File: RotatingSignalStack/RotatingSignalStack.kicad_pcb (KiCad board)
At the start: 2 copper layers, 64.1 x 54 mm, 96 parts, among them IC2 STM32H562RIT6, J1 Conn_01x06, J2 Conn_01x04, J3 RJ45_LED_Shielded, J4 Conn_01x09, SW1 SW_Push, SW5 SW_Push, SW6 SW_Push, SW7 SW_Push, T1 GMG116S1202R, U1 TMAG5273C1QDBVR, U2 AP63203WU-7, U3 SN65HVD232, U4 DP83825I, U5 SG-210STF 50.0000ML0, U6 USBLC6-2SC6, U7 USBLC6-4SC6, U8 OKI-78SR-3.3_1.5-W36-C

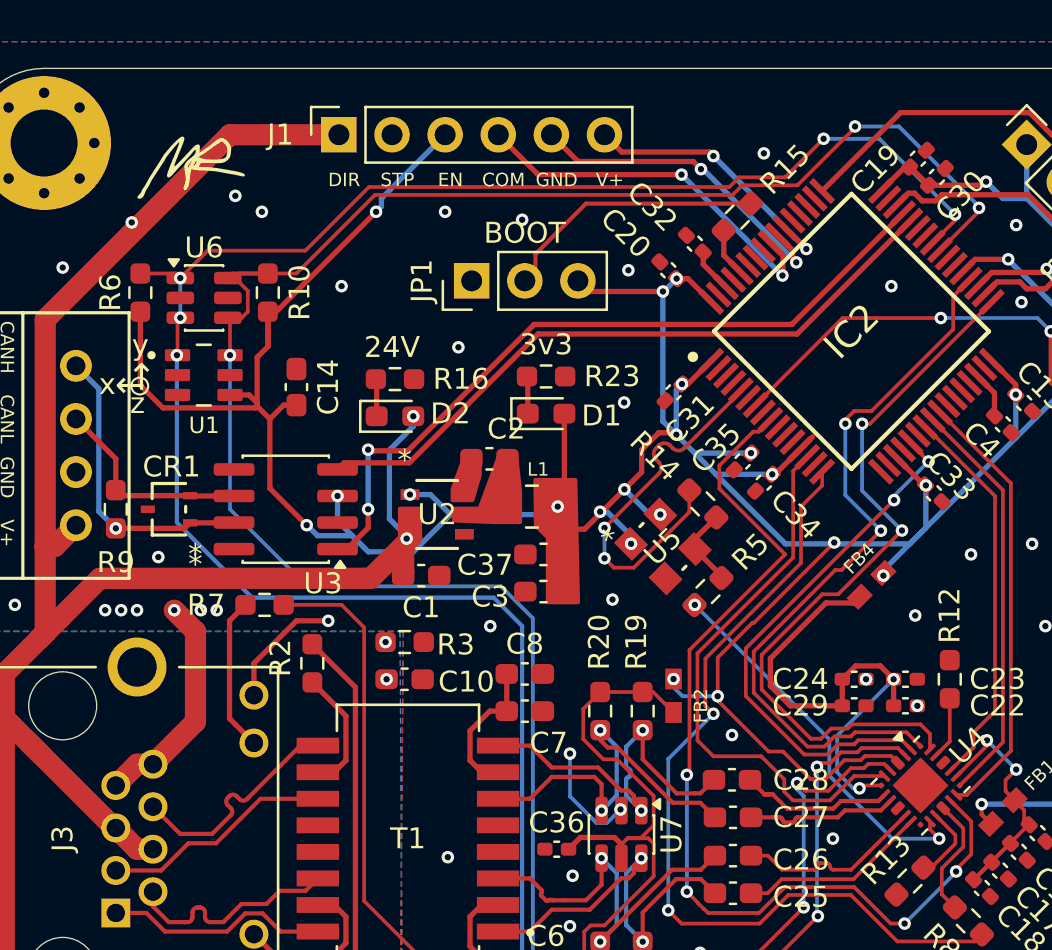
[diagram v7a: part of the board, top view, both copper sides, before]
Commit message: some more vias
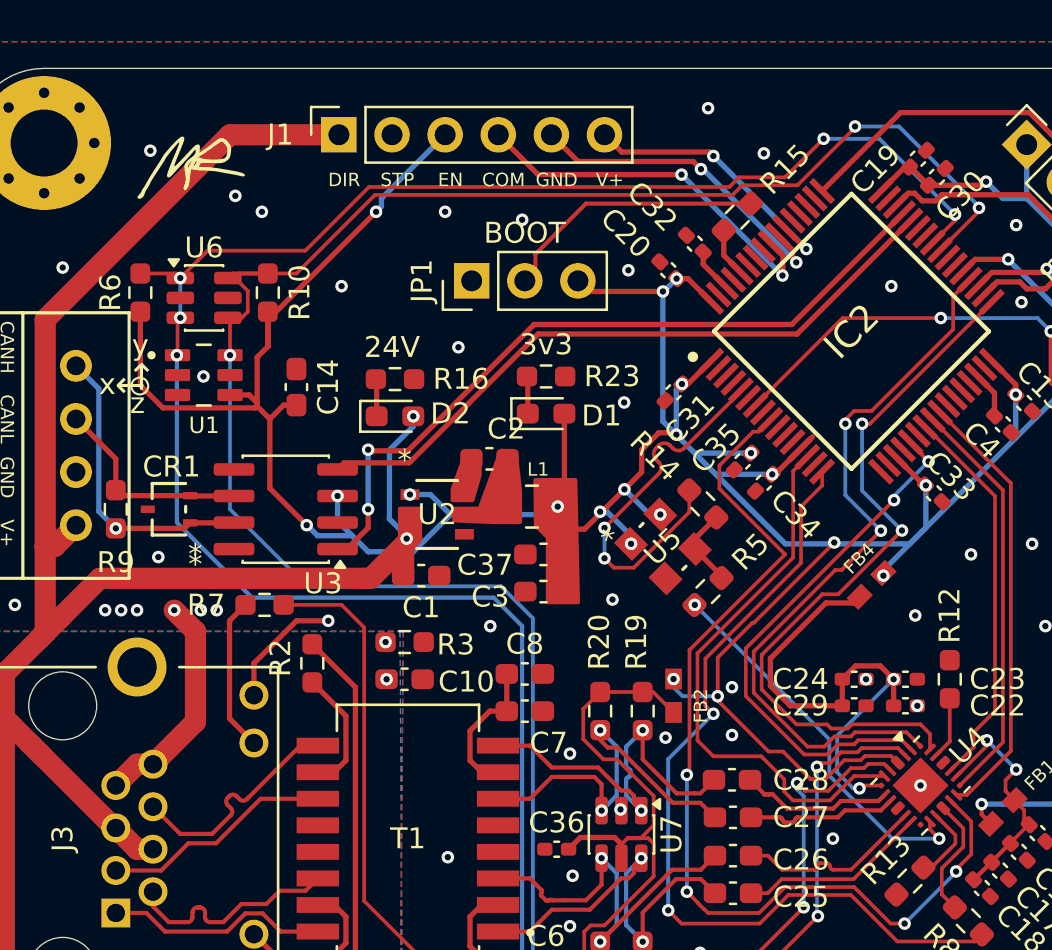
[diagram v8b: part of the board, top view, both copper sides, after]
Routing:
- net GND: track 28.8 -> 23.6 mm, vias 51 -> 56
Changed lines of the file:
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@@
 	)
 	(via
+		(at 161.798 84.709)
+		(size 0.6)
+		(drill 0.3)
+		(layers "F.Cu" "B.Cu")
+		(free yes)
+		(net 1)
+	)
+	(via
 		(at 156.083 80.518)
 		(size 0.6)
@@
 	)
 	(via
+		(at 170.815 89.408)
+		(size 0.6)
+		(drill 0.3)
+		(layers "F.Cu" "B.Cu")
+		(net 1)
+	)
+	(via
 		(at 169.418 65.532)
 		(size 0.6)
@@
 	)
 	(via
-		(at 133.096 62.484)
+		(at 133.985 59.055)
+		(size 0.6)
+		(drill 0.3)
+		(layers "F.Cu" "B.Cu")
+		(free yes)
+		(net 1)
+	)
+	(via
+		(at 136.525 69.85)
 		(size 0.6)
 		(drill 0.3)
@@
 	)
 	(via
-		(at 156.845 64.77)
+		(at 158.623 87.122)
 		(size 0.6)
 		(drill 0.3)
@@
 	)
 	(via
-		(at 137.16 81.026)
+		(at 160.655 57.023)
 		(size 0.6)
 		(drill 0.3)
@@
 	)
 	(via
-		(at 160.274 97.409)
+		(at 156.845 64.77)
 		(size 0.6)
 		(drill 0.3)
@@
 		(net 1)
 	)
-	(segment
-		(start 155.82103 91.1998)
-		(end 155.318055 91.1998)
-		(width 0.1778)
-		(layer "B.Cu")
-		(net 1)
-	)
-	(segment
-		(start 156.466915 90.553915)
-		(end 155.82103 91.1998)
-		(width 0.1778)
-		(layer "B.Cu")
-		(net 1)
-	)
-	(segment
-		(start 154.051 89.932745)
-		(end 154.051 87.884)
-		(width 0.1778)
-		(layer "B.Cu")
+	(via
+		(at 137.16 81.026)
+		(size 0.6)
+		(drill 0.3)
+		(layers "F.Cu" "B.Cu")
+		(free yes)
 		(net 1)
 	)
-	(segment
-		(start 155.318055 91.1998)
-		(end 154.051 89.932745)
-		(width 0.1778)
-		(layer "B.Cu")
+	(via
+		(at 160.274 97.409)
+		(size 0.6)
+		(drill 0.3)
+		(layers "F.Cu" "B.Cu")
+		(free yes)
 		(net 1)
 	)
@@
 	)
 	(segment
-		(start 167.52692 86.483691)
-		(end 167.326192 86.684419)
+		(start 166.116327 80.264326)
+		(end 166.877674 80.264326)
 		(width 0.1778)
 		(layer "F.Cu")
@@
 	)
 	(segment
-		(start 167.52692 86.483691)
+		(start 171.265781 86.937781)
 		(end 170.811691 86.483691)
 		(width 0.1778)
@@
 	)
 	(segment
-		(start 163.217038 83.163615)
-		(end 166.116327 80.264326)
+		(start 167.326192 86.684419)
+		(end 166.542623 86.684419)
 		(width 0.1778)
 		(layer "F.Cu")
@@
 	)
 	(segment
-		(start 171.265781 87.684427)
-		(end 171.265781 86.937781)
+		(start 163.217038 84.818814)
+		(end 163.217038 83.163615)
 		(width 0.1778)
 		(layer "F.Cu")
@@
 	)
 	(segment
-		(start 166.116327 80.264326)
-		(end 166.877674 80.264326)
+		(start 164.885224 86.487)
+		(end 163.217038 84.818814)
 		(width 0.1778)
 		(layer "F.Cu")
@@
 	)
 	(segment
-		(start 171.265781 86.937781)
-		(end 170.811691 86.483691)
+		(start 167.52692 86.483691)
+		(end 167.326192 86.684419)
 		(width 0.1778)
 		(layer "F.Cu")
@@
 	)
 	(segment
-		(start 166.056192 87.17085)
-		(end 166.542623 86.684419)
+		(start 163.217038 83.163615)
+		(end 166.116327 80.264326)
 		(width 0.1778)
 		(layer "F.Cu")
@@
 	)
 	(segment
-		(start 163.217038 84.818814)
-		(end 165.569074 87.17085)
+		(start 166.345204 86.487)
+		(end 164.885224 86.487)
 		(width 0.1778)
 		(layer "F.Cu")
@@
 	)
 	(segment
-		(start 167.326192 86.684419)
-		(end 166.542623 86.684419)
+		(start 171.265781 87.684427)
+		(end 171.265781 86.937781)
 		(width 0.1778)
 		(layer "F.Cu")
@@
 	)
 	(segment
-		(start 168.021 72.110365)
-		(end 168.396936 72.110365)
+		(start 170.811691 86.483691)
+		(end 167.52692 86.483691)
 		(width 0.1778)
 		(layer "F.Cu")
@@
 	)
 	(segment
-		(start 166.056192 87.17085)
-		(end 165.569074 87.17085)
+		(start 168.021 72.110365)
+		(end 168.396936 72.110365)
 		(width 0.1778)
 		(layer "F.Cu")
@@
 	)
 	(segment
-		(start 163.217038 84.818814)
-		(end 163.217038 83.163615)
+		(start 166.542623 86.684419)
+		(end 166.345204 86.487)
 		(width 0.1778)
 		(layer "F.Cu")
